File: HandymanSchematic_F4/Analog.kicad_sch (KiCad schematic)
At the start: 47 parts, among them Q1 BC847, U1 TL074, U2 TL074

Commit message: tweaks to analog circuit
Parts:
- removed unit 5 of U1
- added C11: 47n, Capacitor_SMD:C_0805_2012Metric, symbol Device:C
- added R24: 47k, Resistor_SMD:R_0805_2012Metric, symbol Device:R_US
- added R25: 220k, Resistor_SMD:R_0805_2012Metric, symbol Device:R_US
- added R26: 330k, Resistor_SMD:R_0805_2012Metric, symbol Device:R_US
- added U?: TL074, Package_SO:SOIC-14_3.9x8.7mm_P1.27mm, symbol Amplifier_Operational:TL074
- C?: renamed from C5; value 100n -> 1u
- renumbered R5 to R?
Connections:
- net +9V: now also U?.4 (V+)
- net GND: now also R24.2, U?.11 (V-)
- net TUNE_IN: now also R26.2
- net VG: now also RV1.1, C11.2; no longer RV1.3
- net at U1.10 (+): now also R?.2, R24.1
- net at U1.9 (-): now also R25.2, R26.1
- net at R14.2: now also RV1.3; no longer RV1.1
- net at R10.1, R7.2, R9.1: now also C11.1
- new net: C?.2, R25.1
- new net +3.3V: R?.1
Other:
- moved on the sheet: R5, R9, RV1, U1C

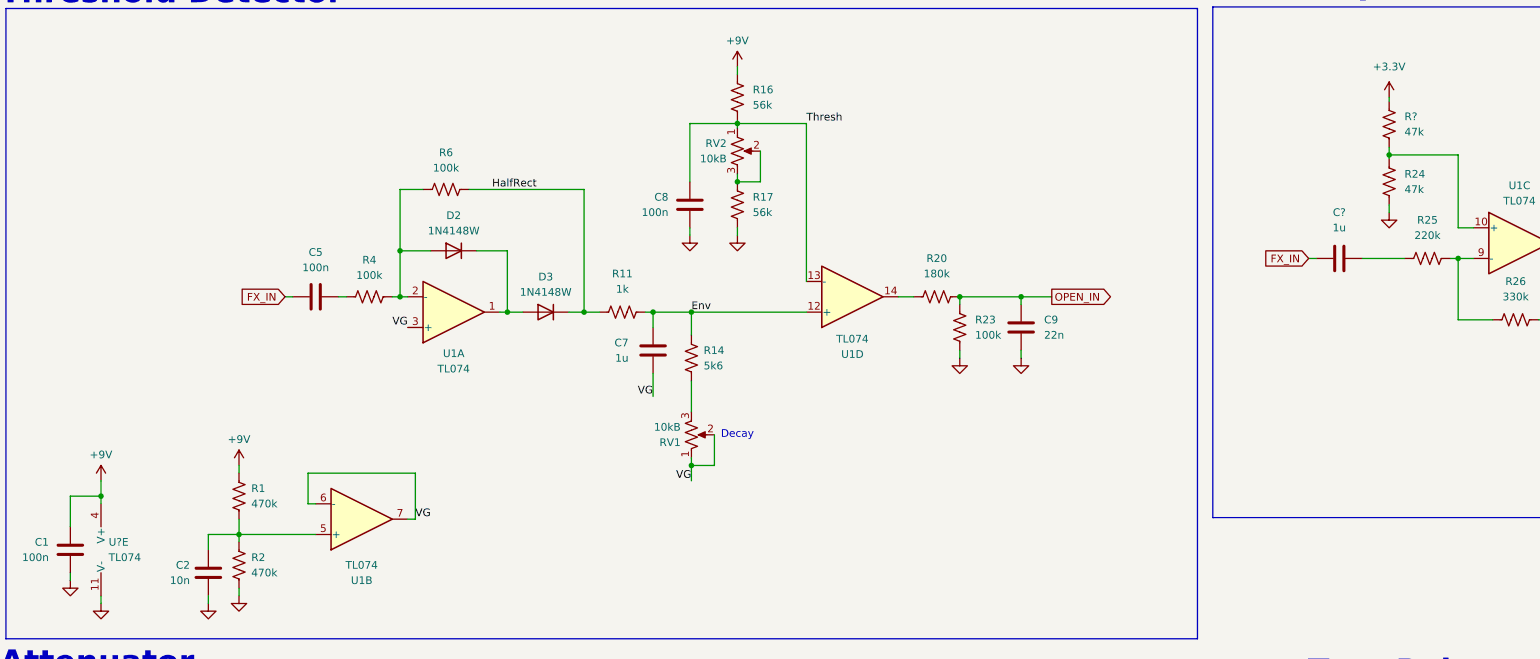
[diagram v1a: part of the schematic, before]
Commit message: F4 wired up on schem, footprints assigned
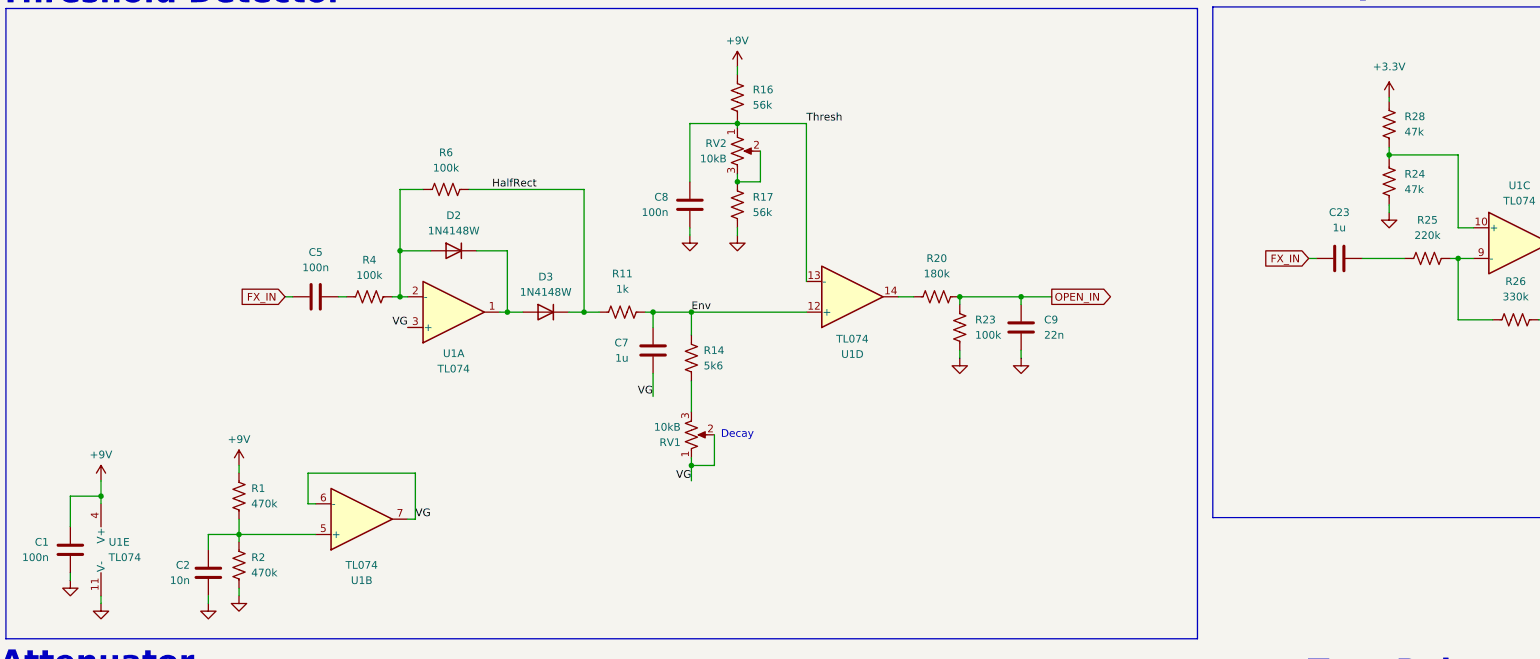
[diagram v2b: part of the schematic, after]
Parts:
- added C23: 1u, Capacitor_SMD:C_0805_2012Metric, symbol Device:C
- added R28: 47k, Resistor_SMD:R_0805_2012Metric, symbol Device:R_US
- C5: renamed from C?; value 1u -> 100n
- gave numbers to parts that had none: 2
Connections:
- net +3.3V: now also R28.1; no longer R5.1
- net FX_IN: now also C23.1
- net at R24.1, U1.10 (+): now also R28.2; no longer R5.2
- net at R25.1: now also C23.2; no longer C5.2
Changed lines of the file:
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@@
 		(dnp no)
 		(fields_autoplaced yes)
-		(property "Reference" "R?"
+		(property "Reference" "R28"
 			(at 251.46 38.7349 0)
 			(effects
@@
 			(project "HandymanSchematic_F4"
 				(path "/bc3da82e-d0a7-49a6-b9ec-ecd2040670ff/3aa5a90d-1712-4ed6-8a31-c8d55dd0f37d"
-					(reference "R?")
+					(reference "R28")
 					(unit 1)
 				)
@@
 		(dnp no)
 		(fields_autoplaced yes)
-		(property "Reference" "U?"
+		(property "Reference" "U1"
 			(at 36.83 109.2199 0)
 			(effects
@@
 			(project "HandymanSchematic_F4"
 				(path "/bc3da82e-d0a7-49a6-b9ec-ecd2040670ff/3aa5a90d-1712-4ed6-8a31-c8d55dd0f37d"
-					(reference "U?")
+					(reference "U1")
 					(unit 5)
 				)
@@
 		(dnp no)
 		(fields_autoplaced yes)
-		(property "Reference" "C?"
+		(property "Reference" "C23"
 			(at 240.665 54.61 90)
 			(effects
@@
 			(project "HandymanSchematic_F4"
 				(path "/bc3da82e-d0a7-49a6-b9ec-ecd2040670ff/3aa5a90d-1712-4ed6-8a31-c8d55dd0f37d"
-					(reference "C?")
-					(unit 1)
-				)
+					(reference "C23")
+					(unit 1)
+				)

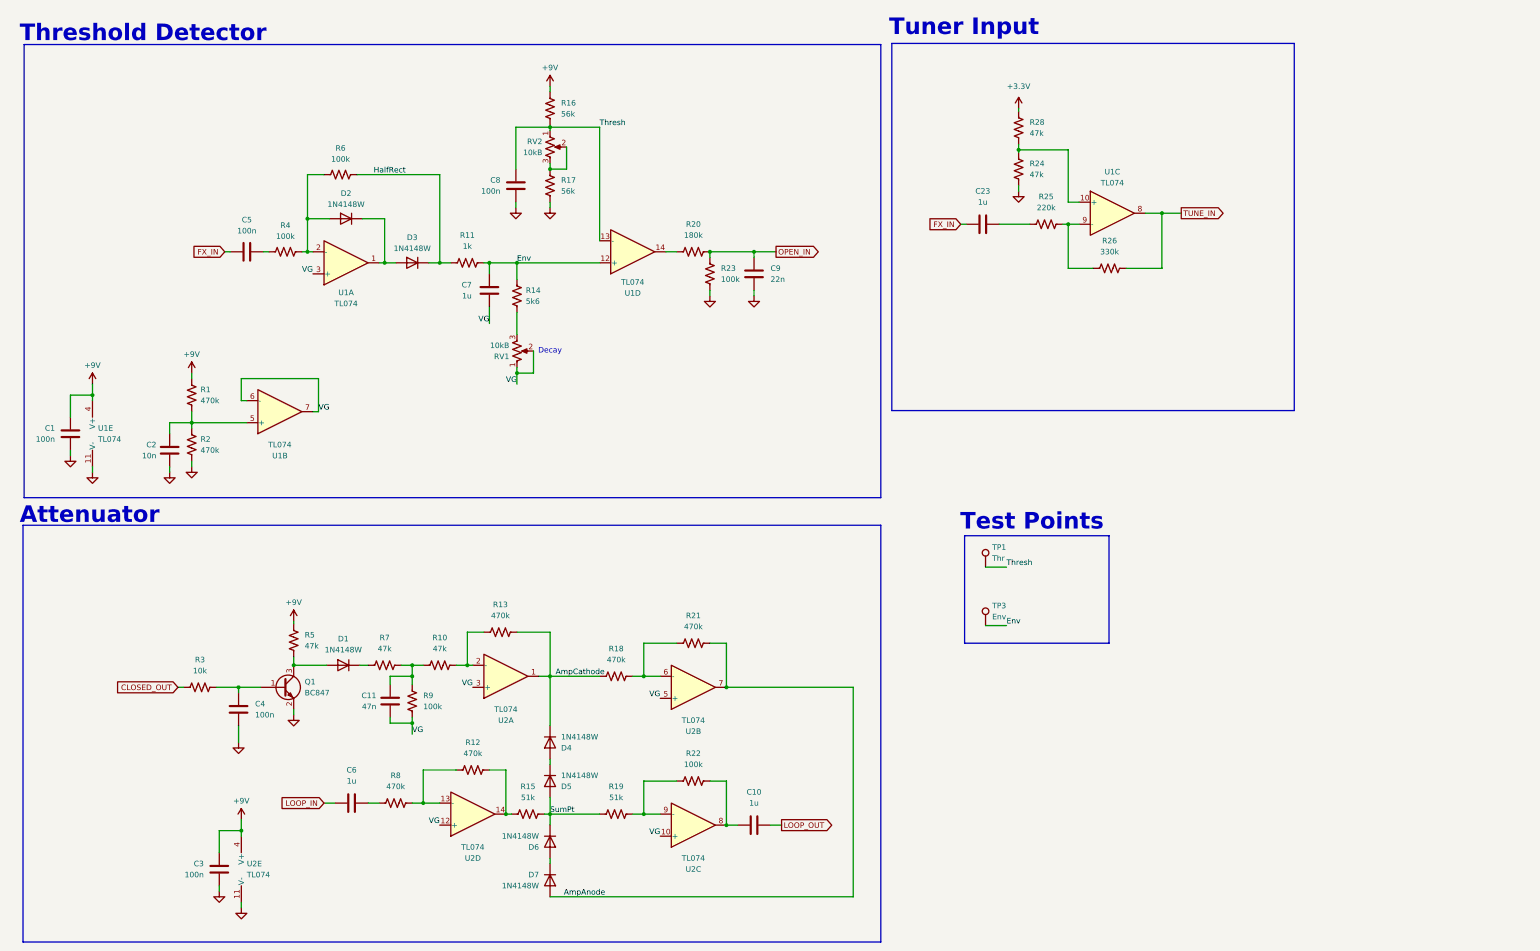
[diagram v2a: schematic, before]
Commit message: switched to firmware env, new layout
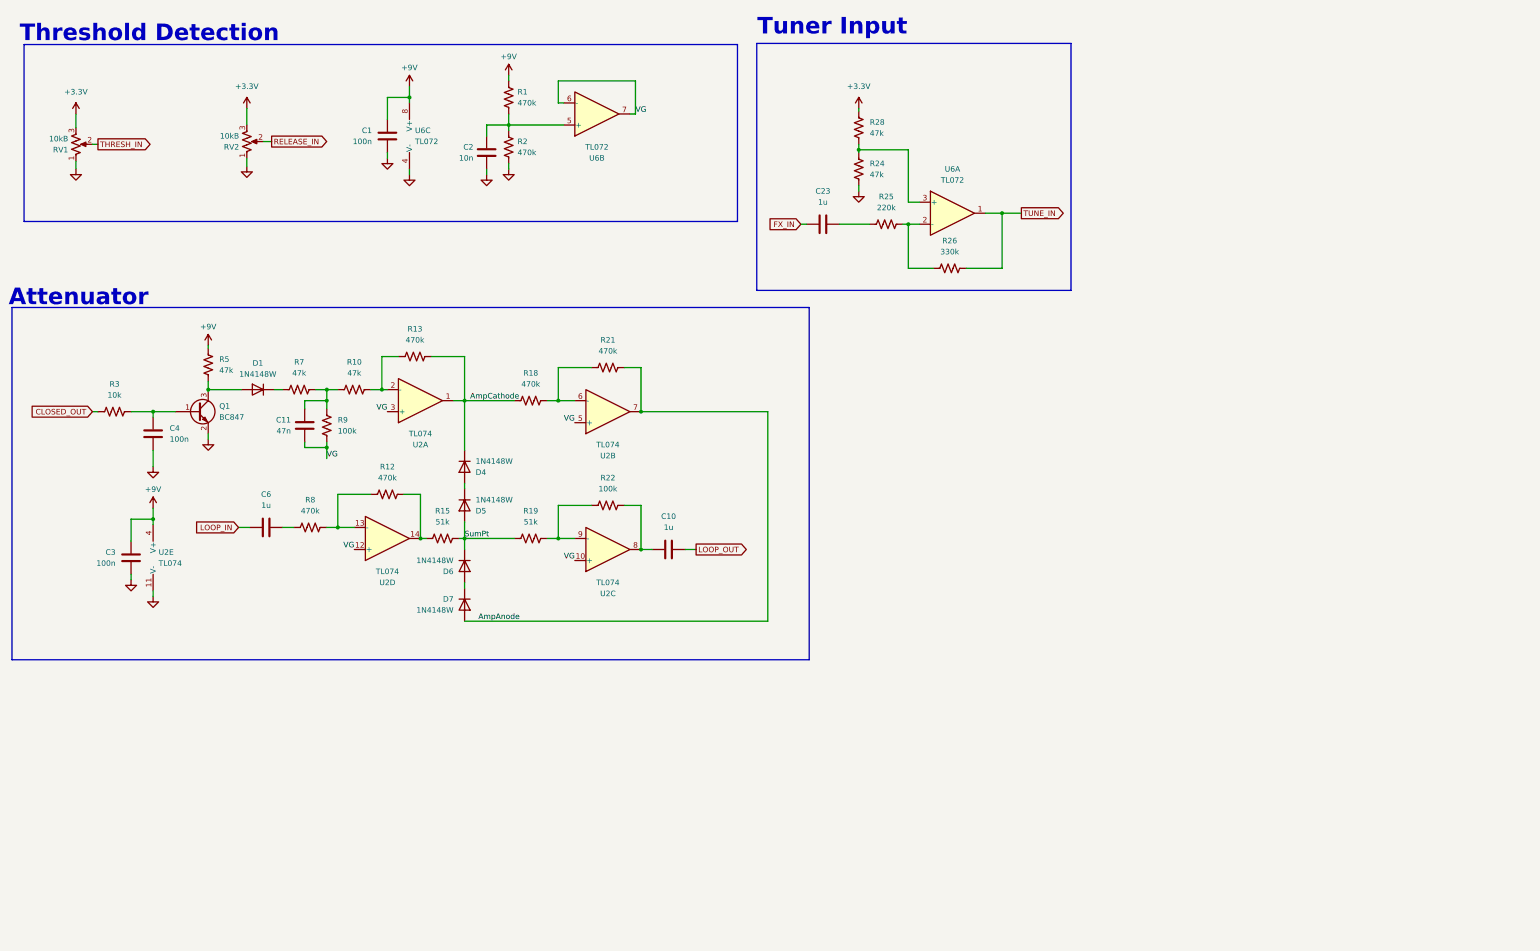
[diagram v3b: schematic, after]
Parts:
- removed C5, C8: 100n, Capacitor_SMD:C_0805_2012Metric, symbol Device:C
- removed C7: 1u, Capacitor_SMD:C_0805_2012Metric, symbol Device:C
- removed C9: 22n, Capacitor_SMD:C_0805_2012Metric, symbol Device:C
- removed D2, D3: 1N4148W, Diode_SMD:D_SOD-123, symbol Diode:1N4148W
- removed R11: 1k, Resistor_SMD:R_0805_2012Metric, symbol Device:R_US
- removed R14: 5k6, Resistor_SMD:R_0805_2012Metric, symbol Device:R_US
- removed R16, R17: 56k, Resistor_SMD:R_0805_2012Metric, symbol Device:R_US
- removed R20: 180k, Resistor_SMD:R_0805_2012Metric, symbol Device:R_US
- removed R23, R4, R6: 100k, Resistor_SMD:R_0805_2012Metric, symbol Device:R_US
- removed TP1: Thr, TestPoint:TestPoint_THTPad_D2.0mm_Drill1.0mm_VAL, symbol Connector:TestPoint
- removed TP3: Env, TestPoint:TestPoint_THTPad_D2.0mm_Drill1.0mm_VAL, symbol Connector:TestPoint
- removed U1: TL074, Package_SO:SOIC-14_3.9x8.7mm_P1.27mm, symbol Amplifier_Operational:TL074
- added U6: TL072, Package_SO:SOIC-8_3.9x4.9mm_P1.27mm, symbol Amplifier_Operational:TL072
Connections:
- net Thresh is gone; now on net GND: RV2.1
- net +3.3V: now also RV1.3, RV2.3
- net +9V: now also U6.8 (V+)
- net GND: now also RV1.1, U6.4 (V-)
- net TUNE_IN: now also U6.1
- net VG: now also U6.6 (-), U6.7; no longer RV1.1, RV1.2
- net at R24.1, R28.2: now also U6.3 (+)
- net at R25.2, R26.1: now also U6.2 (-)
- net at C2.1, R1.2, R2.1: now also U6.5 (+)
- net RELEASE_IN: now reaches RV2.2
- net RELEASE_IN: no longer RV2.3
- new net THRESH_IN: RV1.2
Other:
- note added: "Threshold Detection"
- note removed: "Decay"
- note removed: "Test Points"
- note removed: "Threshold Detector"
- moved on the sheet: C1, C10, C11, C2, C23, C3, C4, C6, D1, D4, D5, D6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

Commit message: prettier routing, DRC passing
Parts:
- added TP1: AC, TestPoint:TestPoint_THTPad_D2.0mm_Drill1.0mm_VAL, symbol Connector:TestPoint
- added TP2: AA, TestPoint:TestPoint_THTPad_D2.0mm_Drill1.0mm_VAL, symbol Connector:TestPoint
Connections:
- net AmpAnode: now also TP2.1
- net AmpCathode: now also TP1.1
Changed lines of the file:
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@@
 	(wire
 		(pts
+			(xy 171.45 90.805) (xy 171.45 89.535)
+		)
+		(stroke
+			(width 0)
+			(type default)
+		)
+	)
+	(wire
+		(pts
+			(xy 173.99 90.805) (xy 171.45 90.805)
+		)
+		(stroke
+			(width 0)
+			(type default)
+		)
+	)
+	(wire
+		(pts
 			(xy 103.505 33.02) (xy 108.585 33.02)
 		)
@@
 	(wire
 		(pts
+			(xy 171.45 99.06) (xy 171.45 97.79)
+		)
+		(stroke
+			(width 0)
+			(type default)
+		)
+	)
+	(wire
+		(pts
 			(xy 89.535 112.395) (xy 89.535 113.665)
 		)
@@
 		)
 	)
+	(wire
+		(pts
+			(xy 173.99 99.06) (xy 171.45 99.06)
+		)
+		(stroke
+			(width 0)
+			(type default)
+		)
+	)
 	(label "VG"
 		(at 103.505 105.41 180)
@@
 	)
 	(label "AmpAnode"
+		(at 173.99 99.06 0)
+		(effects
+			(font
+				(size 1.27 1.27)
+			)
+			(justify left bottom)
+		)
+	)
+	(label "AmpAnode"
 		(at 133.985 153.67 180)
 		(effects
@@
 		)
 	)
+	(label "AmpCathode"
+		(at 173.99 90.805 0)
+		(effects
+			(font
+				(size 1.27 1.27)
+			)
+			(justify left bottom)
+		)
+	)
 	(label "VG"
 		(at 160.655 36.83 0)
@@
 	)
 	(symbol
+		(lib_id "Connector:TestPoint")
+		(at 171.45 89.535 0)
+		(unit 1)
+		(exclude_from_sim no)
+		(in_bom no)
+		(on_board yes)
+		(dnp no)
+		(fields_autoplaced yes)
+		(property "Reference" "TP1"
+			(at 173.355 84.9629 0)
+			(effects
+				(font
+					(size 1.27 1.27)
+				)
+				(justify left)
+			)
+		)
+		(property "Value" "AC"
+			(at 173.355 87.5029 0)
+			(effects
+				(font
+					(size 1.27 1.27)
+				)
+				(justify left)
+			)
+		)
+		(property "Footprint" "TestPoint:TestPoint_THTPad_D2.0mm_Drill1.0mm_VAL"
+			(at 176.53 89.535 0)
+			(effects
+				(font
+					(size 1.27 1.27)
+				)
+				(hide yes)
+			)
+		)
+		(property "Datasheet" "~"
+			(at 176.53 89.535 0)
+			(effects
+				(font
+					(size 1.27 1.27)
+				)
+				(hide yes)
+			)
+		)
+		(property "Description" "test point"
+			(at 171.45 89.535 0)
+			(effects
+				(font
+					(size 1.27 1.27)
+				)
+				(hide yes)
+			)
+		)
+		(pin "1"
+		)
+		(instances
+			(project "HandymanSchematic_F4"
+				(path "/bc3da82e-d0a7-49a6-b9ec-ecd2040670ff/3aa5a90d-1712-4ed6-8a31-c8d55dd0f37d"
+					(reference "TP1")
+					(unit 1)
+				)
+			)
+		)
+	)
+	(symbol
 		(lib_id "Device:R_US")
 		(at 131.445 44.45 0)
@@
 					(unit 1)
 				)
+			)
+		)
+	)
+	(symbol
+		(lib_id "Connector:TestPoint")
+		(at 171.45 97.79 0)
+		(unit 1)
+		(exclude_from_sim no)
+		(in_bom no)
+		(on_board yes)
+		(dnp no)
+		(fields_autoplaced yes)
+		(property "Reference" "TP2"
+			(at 173.355 93.2179 0)
+			(effects
+				(font
+					(size 1.27 1.27)
+				)
+				(justify left)
+			)
+		)
+		(property "Value" "AA"
+			(at 173.355 95.7579 0)
+			(effects
+				(font
+					(size 1.27 1.27)
+				)
+				(justify left)
+			)
+		)
+		(property "Footprint" "TestPoint:TestPoint_THTPad_D2.0mm_Drill1.0mm_VAL"
+			(at 176.53 97.79 0)
+			(effects
+				(font
+					(size 1.27 1.27)
+				)
+				(hide yes)
+			)
+		)
+		(property "Datasheet" "~"
+			(at 176.53 97.79 0)
+			(effects
+				(font
+					(size 1.27 1.27)
+				)
+				(hide yes)
+			)
+		)
+		(property "Description" "test point"
+			(at 171.45 97.79 0)
+			(effects
+				(font
+					(size 1.27 1.27)
+				)
+				(hide yes)
+			)
+		)
+		(pin "1"
+		)
+		(instances
+			(project "HandymanSchematic_F4"
+				(path "/bc3da82e-d0a7-49a6-b9ec-ecd2040670ff/3aa5a90d-1712-4ed6-8a31-c8d55dd0f37d"
+					(reference "TP2")
+					(unit 1)
+				)

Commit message: new prelim routing, DRC passing
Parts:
- removed C2: 10n, Capacitor_SMD:C_0805_2012Metric, symbol Device:C
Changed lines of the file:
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@@
-	(wire
-		(pts
-			(xy 126.365 39.37) (xy 131.445 39.37)
-		)
-		(stroke
-			(width 0)
-			(type default)
-		)
-	)
 	(wire
 		(pts
@@
 	(wire
 		(pts
-			(xy 126.365 49.53) (xy 126.365 50.8)
-		)
-		(stroke
-			(width 0)
-			(type default)
-		)
-	)
-	(wire
-		(pts
 			(xy 84.455 104.775) (xy 84.455 102.87)
 		)
@@
 		(pts
 			(xy 191.135 105.41) (xy 191.135 153.67)
-		)
-		(stroke
-			(width 0)
-			(type default)
-		)
-	)
-	(wire
-		(pts
-			(xy 126.365 41.91) (xy 126.365 39.37)
 		)
 		(stroke
@@
 					(unit 1)
 				)
-			)
-		)
-	)
-	(symbol
-		(lib_id "Device:C")
-		(at 126.365 45.72 0)
-		(unit 1)
-		(exclude_from_sim no)
-		(in_bom yes)
-		(on_board yes)
-		(dnp no)
-		(fields_autoplaced yes)
-		(property "Reference" "C2"
-			(at 123.317 44.4499 0)
-			(effects
-				(font
-					(size 1.27 1.27)
-				)
-				(justify right)
-			)
-		)
-		(property "Value" "10n"
-			(at 123.317 46.9899 0)
-			(effects
-				(font
-					(size 1.27 1.27)
-				)
-				(justify right)
-			)
-		)
-		(property "Footprint" "Capacitor_SMD:C_0805_2012Metric"
-			(at 127.3302 49.53 0)
-			(effects
-				(font
-					(size 1.27 1.27)
-				)
-				(hide yes)
-			)
-		)
-		(property "Datasheet" "~"
-			(at 126.365 45.72 0)
-			(effects
-				(font
-					(size 1.27 1.27)
-				)
-				(hide yes)
-			)
-		)
-		(property "Description" "Unpolarized capacitor"
-			(at 126.365 45.72 0)
-			(effects
-				(font
-					(size 1.27 1.27)
-				)
-				(hide yes)
-			)
-		)
-		(pin "2"
-		)
-		(pin "1"
-		)
-		(instances
-			(project "HandymanSchematic_G0"
-				(path "/bc3da82e-d0a7-49a6-b9ec-ecd2040670ff/3aa5a90d-1712-4ed6-8a31-c8d55dd0f37d"
-					(reference "C2")
-					(unit 1)
-				)
-			)
-			(project "Analog"
-				(path "/d1e2a625-8f99-459b-9c6d-b6439a985a59"
-					(reference "C?")
-					(unit 1)
-				)
-			)
-		)
-	)
-	(symbol
-		(lib_id "power:GND")
-		(at 126.365 50.8 0)
-		(unit 1)
-		(exclude_from_sim no)
-		(in_bom yes)
-		(on_board yes)
-		(dnp no)
-		(fields_autoplaced yes)
-		(property "Reference" "#PWR04"
-			(at 126.365 57.15 0)
-			(effects
-				(font
-					(size 1.27 1.27)
-				)
-				(hide yes)
-			)
-		)
-		(property "Value" "GND"
-			(at 126.365 54.61 0)
-			(effects
-				(font
-					(size 1.27 1.27)
-				)
-				(hide yes)
-			)
-		)
-		(property "Footprint" ""
-			(at 126.365 50.8 0)
-			(effects
-				(font
-					(size 1.27 1.27)
-				)
-				(hide yes)
-			)
-		)
-		(property "Datasheet" ""
-			(at 126.365 50.8 0)
-			(effects
-				(font
-					(size 1.27 1.27)
-				)
-				(hide yes)
-			)
-		)
-		(property "Description" "Power symbol creates a global label with name \"GND\" , ground"
-			(at 126.365 50.8 0)
-			(effects
-				(font
-					(size 1.27 1.27)
-				)
-				(hide yes)
-			)
-		)
-		(pin "1"
-		)
-		(instances
-			(project "HandymanSchematic_G0"
-				(path "/bc3da82e-d0a7-49a6-b9ec-ecd2040670ff/3aa5a90d-1712-4ed6-8a31-c8d55dd0f37d"
-					(reference "#PWR04")
-					(unit 1)
-				)
-			)
-			(project "Analog"
-				(path "/d1e2a625-8f99-459b-9c6d-b6439a985a59"
-					(reference "#PWR?")
-					(unit 1)
-				)

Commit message: mirroring fixed, changed some resistor values
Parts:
- R25: value 220k -> 100k
- R26: value 330k -> 470k
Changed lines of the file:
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@@
 			)
 		)
-		(property "Value" "220k"
+		(property "Value" "100k"
 			(at 218.44 58.42 90)
 			(effects
@@
 			)
 		)
-		(property "Value" "330k"
+		(property "Value" "470k"
 			(at 233.045 68.58 90)
 			(effects
